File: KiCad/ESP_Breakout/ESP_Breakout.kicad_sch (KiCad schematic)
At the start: 14 parts, among them J1 Conn_01x15_Socket, J2 Conn_01x15_Socket

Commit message: Worked on schematic
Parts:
- added J3, J4, J5, J6: Conn_01x03_Pin, symbol Connector:Conn_01x03_Pin
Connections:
- net GND: now also J3.3 (Pin_3), J4.3 (Pin_3), J5.3 (Pin_3), J6.3 (Pin_3)
- net Turn_Ena+: now reaches J_Turn3.2
- net Turn_Ena+: now also J2.7 (Pin_7), J_Turn1.2, J_Turn2.2, J_Turn4.2
- net Turn3_Dir+: now reaches J_Turn3.4
- net Turn3_Dir+: now also J2.6 (Pin_6)
- net Turn3_Pul+: now reaches J_Turn3.6
- net Turn3_Pul+: now also J2.5 (Pin_5)
- net Turn4_Dir+: now reaches J_Turn4.4
- net Turn4_Dir+: now also J2.11 (Pin_11)
- net Turn4_Pul+: now reaches J_Turn4.6
- net Turn4_Pul+: now also J2.14 (Pin_14)
- net Drive_Ena+: now reaches J_Drive4.2
- net Drive_Ena+: now also J1.11 (Pin_11), J_Drive1.2, J_Drive2.2, J_Drive3.2
- net at J_Drive4.3: now also J6.2 (Pin_2)
- net Drive_Dir+: now reaches J_Drive4.4
- net Drive_Dir+: now also J1.12 (Pin_12), J_Drive1.4, J_Drive2.4, J_Drive3.4
- net Drive_Pul+: now reaches J_Drive4.6
- net Drive_Pul+: now also J1.13 (Pin_13), J_Drive1.6, J_Drive2.6, J_Drive3.6
- net Lift_Ena+: now reaches J_Lift3.2
- net Lift_Ena+: now also J1.8 (Pin_8), J_Lift1.2, J_Lift2.2, J_Lift4.2
- net Lift_Dir+: now reaches J_Lift3.4
- net Lift_Dir+: now also J1.9 (Pin_9), J_Lift1.4, J_Lift2.4, J_Lift4.4
- net Lift_Pul+: now reaches J_Lift3.6
- net Lift_Pul+: now also J1.10 (Pin_10), J_Lift1.6, J_Lift2.6, J_Lift4.6
- net Turn2_Dir+: now reaches J_Turn2.4
- net Turn2_Dir+: now also J2.4 (Pin_4)
- net Turn2_Pul+: now reaches J_Turn2.6
- net Turn2_Pul+: now also J2.3 (Pin_3)
- net at J_Drive2.3: now also J4.2 (Pin_2)
- net at J_Drive1.3: now also J3.2 (Pin_2)
- net at J_Drive3.3: now also J5.2 (Pin_2)
- net Turn1_Dir+: now reaches J_Turn1.4
- net Turn1_Dir+: now also J1.6 (Pin_6)
- net Turn1_Pul+: now reaches J_Turn1.6
- net Turn1_Pul+: now also J1.7 (Pin_7)
- new net +5V: J3.1 (Pin_1), J4.1 (Pin_1), J5.1 (Pin_1), J6.1 (Pin_1)
- no-connect marks 0 -> 4
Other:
- moved on the sheet: J1, J2

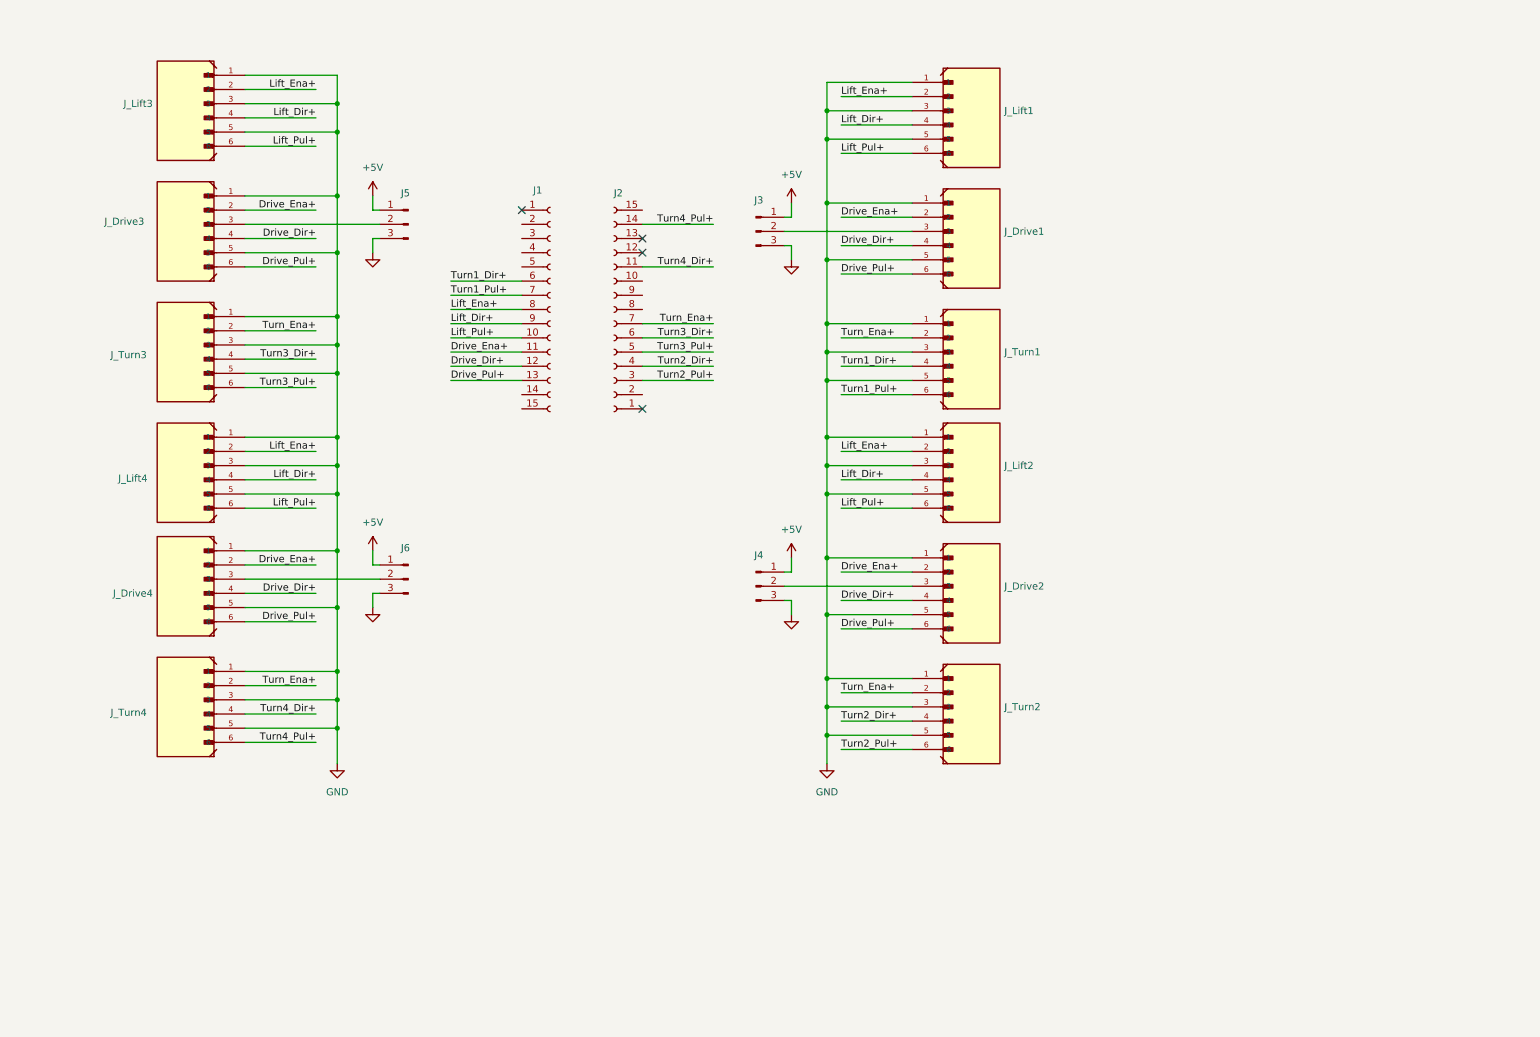
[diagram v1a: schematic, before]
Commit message: import esp32 devkit
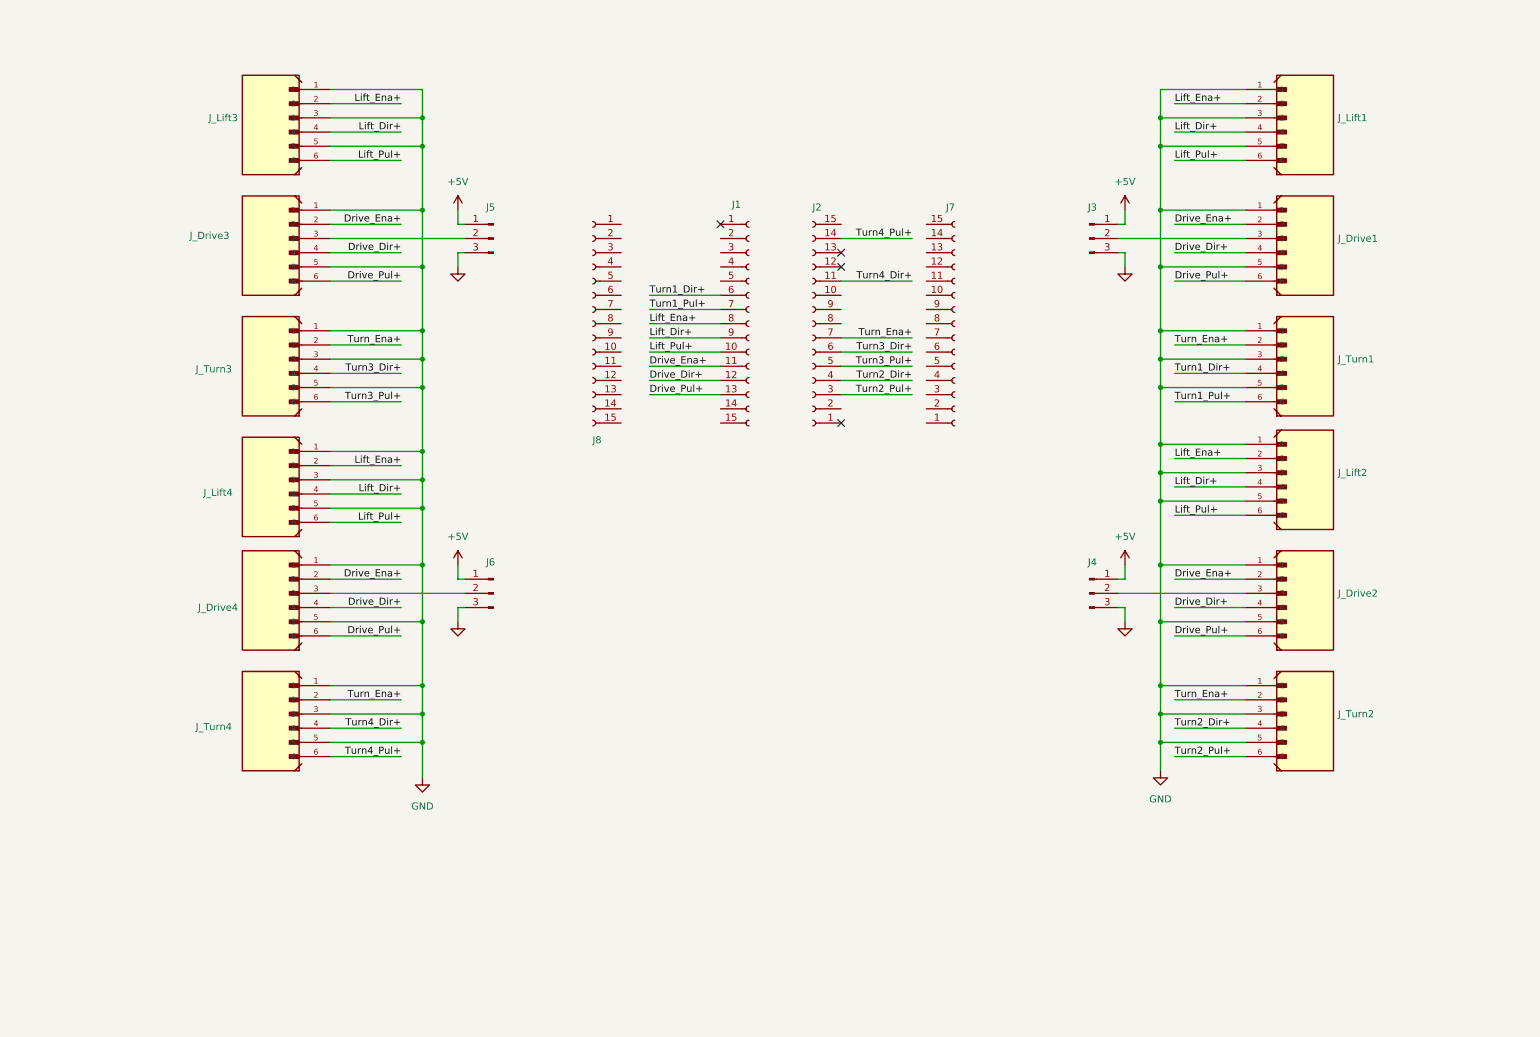
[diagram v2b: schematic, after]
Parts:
- added J7, J8: Conn_01x15_Socket, symbol Connector:Conn_01x15_Socket
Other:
- moved on the sheet: J1, J2, J3, J4, J5, J6, J_Drive1, J_Drive2, J_Drive3, J_Drive4, J_Lift1, J_Lift2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

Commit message: update
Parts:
- removed J7, J8: Conn_01x15_Socket, symbol Connector:Conn_01x15_Socket
- added U1: ~, symbol seniorDesign:ESP32_DEVKIT_V1
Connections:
- net +5V is gone; now on net +3.3V: J3.1 (Pin_1), J4.1 (Pin_1), J5.1 (Pin_1), J6.1 (Pin_1)
- net GND: now also J1.14 (Pin_14)
- net +3.3V: now reaches J2.1 (Pin_1)
- no-connect marks 4 -> 43
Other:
- moved on the sheet: J3, J4, J5, J6, J_Drive1, J_Drive2, J_Drive3, J_Drive4, J_Lift1, J_Lift2, J_Lift3, J_Lift4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

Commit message: footprint assignments
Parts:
- J1, J2: footprint (none) -> Connector_PinSocket_2.54mm:PinSocket_1x15_P2.54mm_Vertical
- J3, J4, J5, J6: footprint (none) -> Connector_PinHeader_1.00mm:PinHeader_1x03_P1.00mm_Vertical
- J_Drive1, J_Drive2, J_Drive3, J_Drive4, J_Lift1, J_Lift2, J_Lift3, J_Lift4, J_Turn1, J_Turn2, J_Turn3, J_Turn4: footprint B6B-PH-K-S:JST_B6B-PH-K-S -> Connector_JST:JST_PH_B6B-PH-K_1x06_P2.00mm_Vertical
- U1: footprint (none) -> seniorDesign:MODULE_ESP32_DEVKIT_V1
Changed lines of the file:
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@@
 			)
 		)
-		(property "Footprint" "B6B-PH-K-S:JST_B6B-PH-K-S"
+		(property "Footprint" "Connector_JST:JST_PH_B6B-PH-K_1x06_P2.00mm_Vertical"
 			(at 27.94 82.55 0)
 			(effects
@@
 			)
 		)
-		(property "Footprint" "B6B-PH-K-S:JST_B6B-PH-K-S"
+		(property "Footprint" "Connector_JST:JST_PH_B6B-PH-K_1x06_P2.00mm_Vertical"
 			(at 27.94 146.05 0)
 			(effects
@@
 			)
 		)
-		(property "Footprint" "B6B-PH-K-S:JST_B6B-PH-K-S"
+		(property "Footprint" "Connector_JST:JST_PH_B6B-PH-K_1x06_P2.00mm_Vertical"
 			(at 27.94 124.46 0)
 			(effects
@@
 			)
 		)
-		(property "Footprint" ""
+		(property "Footprint" "Connector_PinHeader_1.00mm:PinHeader_1x03_P1.00mm_Vertical"
 			(at 228.6 53.34 0)
 			(effects
@@
 			)
 		)
-		(property "Footprint" "B6B-PH-K-S:JST_B6B-PH-K-S"
+		(property "Footprint" "Connector_JST:JST_PH_B6B-PH-K_1x06_P2.00mm_Vertical"
 			(at 27.94 39.37 0)
 			(effects
@@
 			)
 		)
-		(property "Footprint" "B6B-PH-K-S:JST_B6B-PH-K-S"
+		(property "Footprint" "Connector_JST:JST_PH_B6B-PH-K_1x06_P2.00mm_Vertical"
 			(at 266.7 140.97 0)
 			(effects
@@
 			)
 		)
-		(property "Footprint" "B6B-PH-K-S:JST_B6B-PH-K-S"
+		(property "Footprint" "Connector_JST:JST_PH_B6B-PH-K_1x06_P2.00mm_Vertical"
 			(at 266.7 119.38 0)
 			(effects
@@
 			)
 		)
-		(property "Footprint" "B6B-PH-K-S:JST_B6B-PH-K-S"
+		(property "Footprint" "Connector_JST:JST_PH_B6B-PH-K_1x06_P2.00mm_Vertical"
 			(at 266.7 55.88 0)
 			(effects
@@
 			)
 		)
-		(property "Footprint" "B6B-PH-K-S:JST_B6B-PH-K-S"
+		(property "Footprint" "Connector_JST:JST_PH_B6B-PH-K_1x06_P2.00mm_Vertical"
 			(at 27.94 60.96 0)
 			(effects
@@
 			)
 		)
-		(property "Footprint" "B6B-PH-K-S:JST_B6B-PH-K-S"
+		(property "Footprint" "Connector_JST:JST_PH_B6B-PH-K_1x06_P2.00mm_Vertical"
 			(at 266.7 77.47 0)
 			(effects
@@
 			)
 		)
-		(property "Footprint" ""
+		(property "Footprint" "Connector_PinHeader_1.00mm:PinHeader_1x03_P1.00mm_Vertical"
 			(at 67.31 121.92 0)
 			(effects
@@
 			)
 		)
-		(property "Footprint" ""
+		(property "Footprint" "Connector_PinHeader_1.00mm:PinHeader_1x03_P1.00mm_Vertical"
 			(at 67.31 58.42 0)
 			(effects
@@
 			)
 		)
-		(property "Footprint" ""
+		(property "Footprint" "seniorDesign:MODULE_ESP32_DEVKIT_V1"
 			(at 129.54 173.99 0)
 			(effects
@@
 			)
 		)
-		(property "Footprint" "B6B-PH-K-S:JST_B6B-PH-K-S"
+		(property "Footprint" "Connector_JST:JST_PH_B6B-PH-K_1x06_P2.00mm_Vertical"
 			(at 266.7 34.29 0)
 			(effects
@@
 			)
 		)
-		(property "Footprint" ""
+		(property "Footprint" "Connector_PinSocket_2.54mm:PinSocket_1x15_P2.54mm_Vertical"
 			(at 143.51 71.12 0)
 			(effects
@@
 			)
 		)
-		(property "Footprint" "B6B-PH-K-S:JST_B6B-PH-K-S"
+		(property "Footprint" "Connector_JST:JST_PH_B6B-PH-K_1x06_P2.00mm_Vertical"
 			(at 266.7 97.79 0)
 			(effects
@@
 			)
 		)
-		(property "Footprint" ""
+		(property "Footprint" "Connector_PinHeader_1.00mm:PinHeader_1x03_P1.00mm_Vertical"
 			(at 228.6 116.84 0)
 			(effects
@@
 			)
 		)
-		(property "Footprint" "B6B-PH-K-S:JST_B6B-PH-K-S"
+		(property "Footprint" "Connector_JST:JST_PH_B6B-PH-K_1x06_P2.00mm_Vertical"
 			(at 27.94 104.14 0)
 			(effects
@@
 			)
 		)
-		(property "Footprint" ""
+		(property "Footprint" "Connector_PinSocket_2.54mm:PinSocket_1x15_P2.54mm_Vertical"
 			(at 154.94 71.12 0)
 			(effects

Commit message: starting pcb layout
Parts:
- added J7, J8: Conn_01x15_Socket, Connector_PinSocket_2.54mm:PinSocket_1x15_P2.54mm_Vertical, symbol Connector:Conn_01x15_Socket
- J3, J4, J5, J6: footprint Connector_PinHeader_1.00mm:PinHeader_1x03_P1.00mm_Vertical -> Connector_PinHeader_2.54mm:PinHeader_1x03_P2.54mm_Vertical
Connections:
- net +3.3V: now also J2.2 (Pin_2), J7.2 (Pin_2); no longer J2.1 (Pin_1)
- net Drive_Dir+: now also J8.12 (Pin_12)
- net Drive_Ena+: now also J8.11 (Pin_11)
- net Drive_Pul+: now also J8.13 (Pin_13)
- net GND: now also J2.1 (Pin_1), J7.1 (Pin_1); no longer J1.14 (Pin_14)
- net Lift_Dir+: now also J8.9 (Pin_9)
- net Lift_Ena+: now also J8.8 (Pin_8)
- net Lift_Pul+: now also J8.10 (Pin_10)
- net Turn1_Dir+: now also J8.6 (Pin_6)
- net Turn1_Pul+: now also J8.7 (Pin_7)
- net Turn2_Dir+: now also J7.4 (Pin_4)
- net Turn2_Pul+: now also J7.3 (Pin_3)
- net Turn3_Dir+: now also J7.6 (Pin_6)
- net Turn3_Pul+: now also J7.5 (Pin_5)
- net Turn4_Dir+: now also J7.11 (Pin_11)
- net Turn4_Pul+: now also J7.14 (Pin_14)
- net Turn_Ena+: now also J7.7 (Pin_7)
- net at J1.1 (Pin_1): now also J8.1 (Pin_1)
- net at J1.15 (Pin_15): now also J8.15 (Pin_15)
- net at J1.2 (Pin_2): now also J8.2 (Pin_2)
- net at J1.3 (Pin_3): now also J8.3 (Pin_3)
- net at J1.4 (Pin_4): now also J8.4 (Pin_4)
- net at J1.5 (Pin_5): now also J8.5 (Pin_5)
- net at J2.10 (Pin_10): now also J7.10 (Pin_10)
- net at J2.12 (Pin_12): now also J7.12 (Pin_12)
- net at J2.13 (Pin_13): now also J7.13 (Pin_13)
- net at J2.15 (Pin_15): now also J7.15 (Pin_15)
- net at J2.8 (Pin_8): now also J7.8 (Pin_8)
- net at J2.9 (Pin_9): now also J7.9 (Pin_9)
- new net: J1.14 (Pin_14), J8.14 (Pin_14)
- no-connect marks 43 -> 30
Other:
- moved on the sheet: J1, J2, J3, J4, J5, J6, J_Drive1, J_Drive2, J_Drive3, J_Drive4, J_Lift1, J_Lift2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

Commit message: start of pheonix
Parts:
- added H1, H2, H3, H4: MountingHole, MountingHole:MountingHole_2.5mm, symbol Mechanical:MountingHole
